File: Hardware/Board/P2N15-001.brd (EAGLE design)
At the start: 72 x 72 mm, 30 parts, among them IC1 TLC5941NT, IC2 LTC485N, IC3 74LS07N, IC4 LTC485N

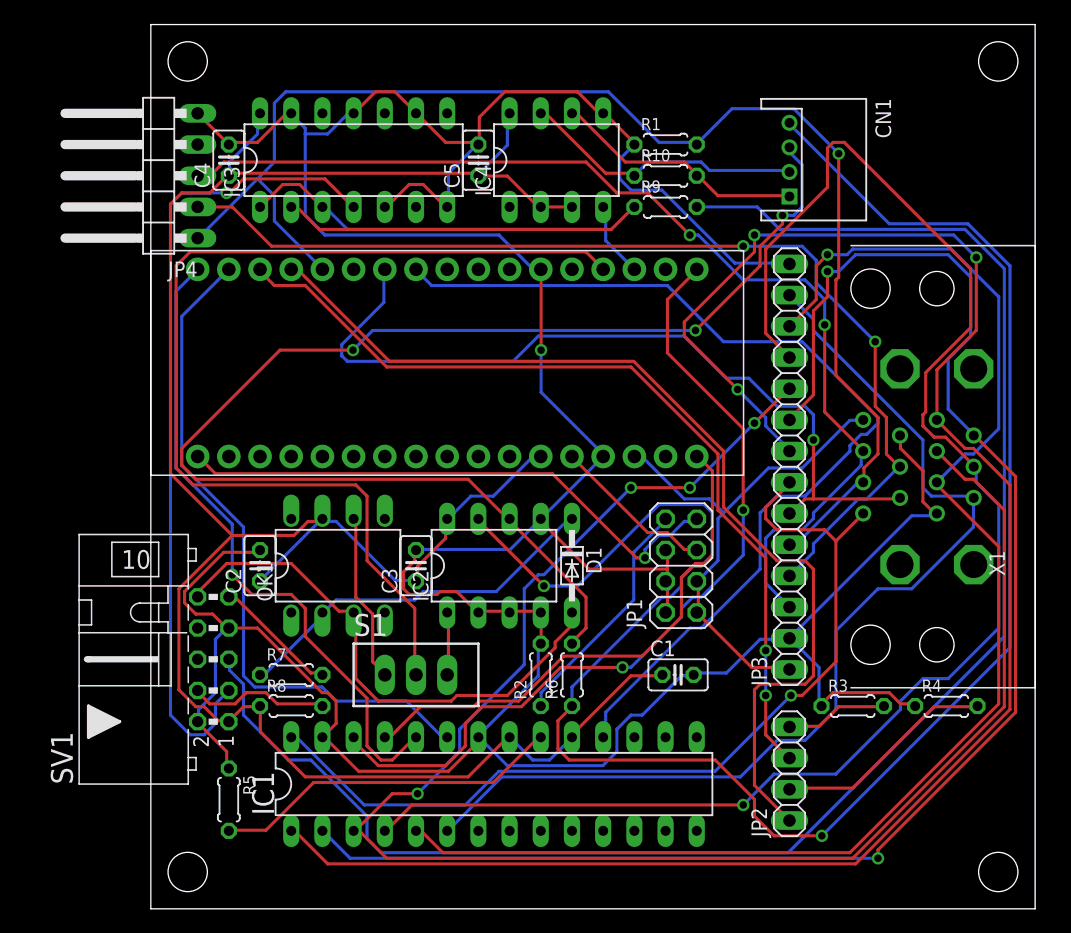
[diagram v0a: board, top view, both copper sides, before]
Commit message: Attached LED pattern to GPIO pins.
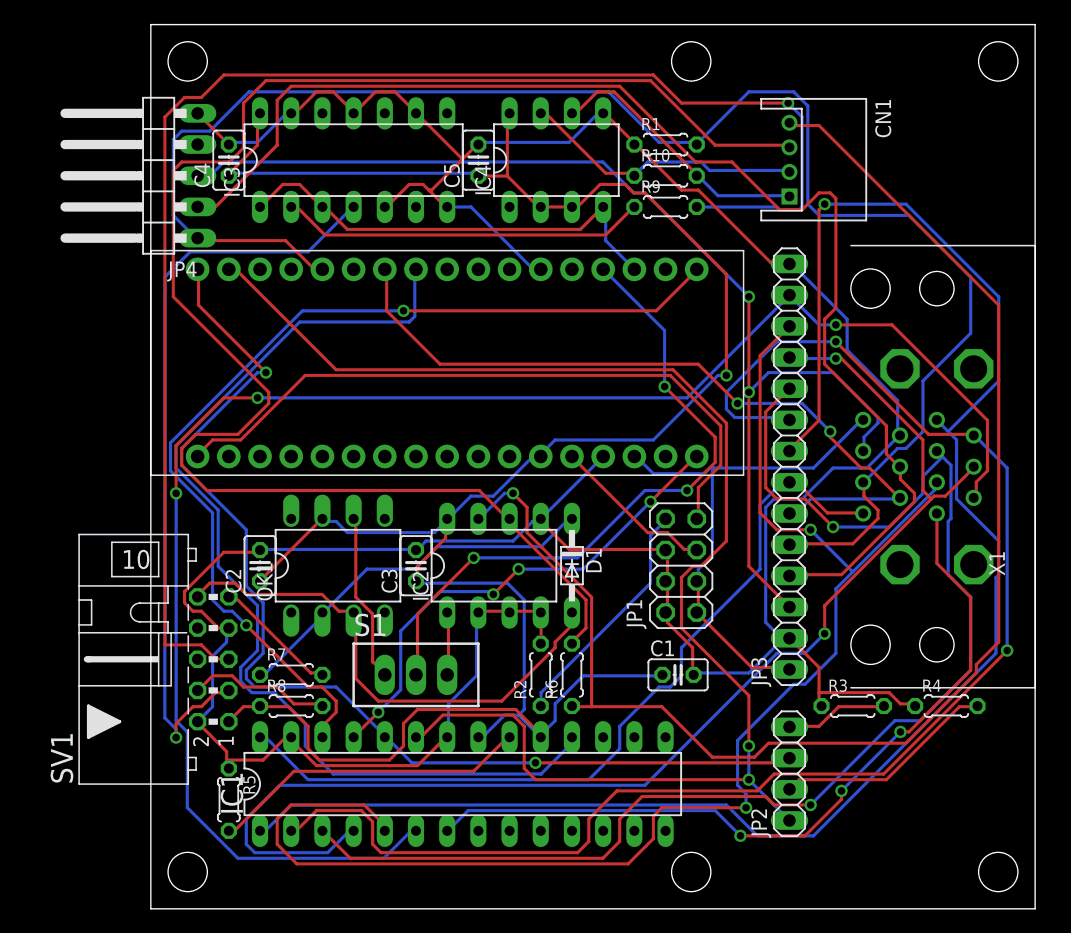
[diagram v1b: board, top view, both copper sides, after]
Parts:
- moved IC1 2.54 mm to (25.4, 10.2)
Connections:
- removed net N$5: JP2.3, MC1.P$3
- new net N$8: IC1.7, X1.14
- net GND: no longer X1.14
- net GPIO1: now also JP2.1
- net GPIO2: now also JP2.3
- net N$3: no longer JP2.1
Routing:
- net N$3: track 81.2 -> 0.00 mm
- net N$5: track 70.8 -> 0.00 mm, vias 2 -> 0
- net N$8: track 0.00 -> 64.0 mm, vias 0 -> 3
- net GPIO1: track 55.5 -> 115.7 mm, vias 0 -> 2
- net N$29: track 83.9 -> 133.3 mm, vias 0 -> 3
- net GND: track 316.0 -> 269.4 mm, vias 1 -> 0
- net GPIO2: track 53.1 -> 89.5 mm, vias 1 -> 2
- net RX-: track 150.4 -> 115.1 mm, vias 2 -> 1
- net RX: track 85.0 -> 53.9 mm, vias 0 -> 3
- net ANLG2: track 137.6 -> 109.3 mm, vias 4 -> 2
- net ANLG3: track 127.3 -> 103.1 mm, vias 1 -> 2
- net RX+: track 108.4 -> 131.6 mm, vias 3 -> 0
- net PD: track 110.9 -> 133.5 mm, vias 1 -> 0
- net USBD-: track 84.9 -> 103.9 mm, vias 2 -> 0
- net RETURN: track 137.1 -> 119.5 mm, vias 0 -> 1
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
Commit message: Added LED monitors to P2N15.
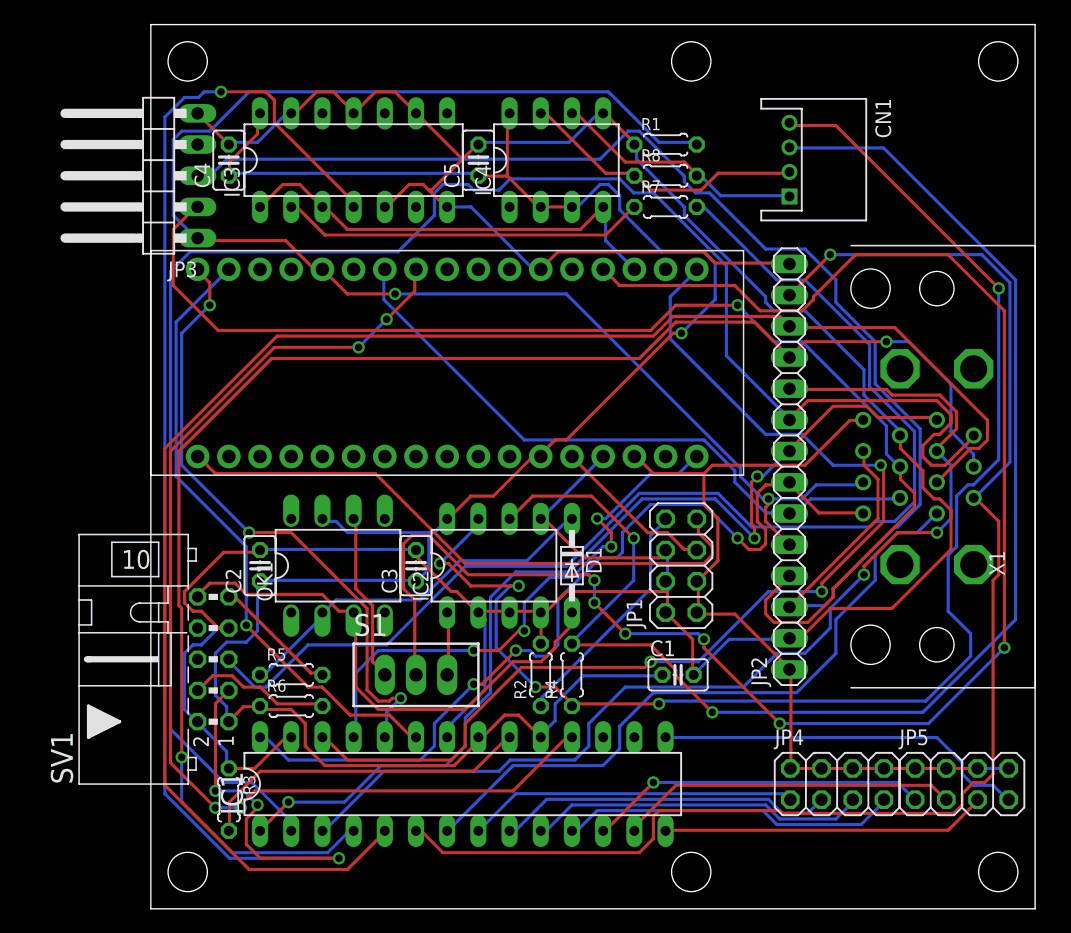
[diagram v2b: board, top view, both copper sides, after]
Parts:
- removed R10: 120, resistor:0204/5
- removed R9: 220, resistor:0204/5
- added JP5: (no value), pinhead:2X04
- JP2: device pinhead:1X04 -> pinhead:1X14
- JP3: device pinhead:1X14 -> pinhead:1X05/90
- JP4: device pinhead:1X05/90 -> pinhead:2X04
- R3: value 330 -> 4.7k
- R4: value 330 -> 120
- R5: value 4.7k -> 220
- R6: value 120 -> 220
- R8: value 220 -> 120
- moved JP4 74.7 mm to (55.9, 10.2), turned to 0 degrees
- moved JP3 57.1 mm to (0.00, 59.7)
- moved R8 52.9 mm to (41.9, 59.7)
- moved R3 51.4 mm to (6.35, 8.89), turned to 270 degrees
- moved R7 48.8 mm to (41.9, 57.1)
- moved R4 30.6 mm to (34.3, 19.1), turned to 90 degrees
- moved JP2 25.0 mm to (52.0, 36.0)
- moved R6 23.0 mm to (11.4, 16.5), turned to 0 degrees
- moved R5 11.4 mm to (11.4, 19.1), turned to 0 degrees
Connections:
- removed net N$6: JP2.2, R4.2
- removed net N$7: JP2.4, R3.2
- new net LED0: IC1.8, JP4.1
- new net LED1: IC1.9, JP4.3
- new net LED2: IC1.10, JP4.5
- new net LED3: IC1.11, JP4.7
- new net LED4: IC1.12, JP5.1
- new net LED5: IC1.13, JP5.3
- new net LED6: IC1.14, JP5.5
- new net LED7: IC1.15, JP5.7
- net ANLG0: now also JP2.8; no longer JP3.8
- net ANLG1: now also JP2.9; no longer JP3.9
- net ANLG2: now also JP2.10; no longer JP3.10
- net ANLG3: now also JP2.11; no longer JP3.11
- net CD: now also JP2.6; no longer JP3.6
- net GND: now also JP2.14, JP2.2, JP3.5; no longer JP3.14, JP3.2, JP4.5, R4.1, R5.1
- net GPIO1: no longer JP2.1
- net GPIO2: no longer JP2.3
- net N$1: now also JP2.7; no longer JP3.7
- net N$15: now also R5.1; no longer R7.1
- net N$2: now also R7.1; no longer R9.1
- net N$28: now also JP2.12; no longer JP3.12
- net N$29: now also JP2.13; no longer JP3.13
- net N$4: now also R3.2; no longer R5.2
- net PD: now also JP2.5, JP3.1; no longer JP3.5, JP4.1
- net RETURN: now also R7.2; no longer R9.2
- net RX+: now also R4.2; no longer R6.2
- net RX-: now also R4.1; no longer R6.1
- net RXA: now also R5.2; no longer R7.2
- net SEND: now also R6.2; no longer R8.2
- net TX+: now also R8.2; no longer R10.2
- net TX-: now also R8.1; no longer R10.1
- net USBD+: now also JP2.3; no longer JP4.3
- net USBD-: now also JP2.4, JP3.2; no longer JP3.4, JP4.2
- net VCC: now also R6.1; no longer R8.1
- net VDD: now also JP2.1, JP4.2, JP4.4, JP4.6, JP4.8, JP5.2, JP5.4, JP5.6, JP5.8; no longer JP3.1
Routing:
- net RX: track 53.9 -> 136.1 mm, vias 3 -> 6
- net GPIO1: track 115.7 -> 50.8 mm, vias 2 -> 1
- net ANLG0: track 140.4 -> 81.5 mm, vias 1 -> 3
- net RAWTX: track 62.2 -> 117.0 mm, vias 1 -> 4
- net GPIO2: track 89.5 -> 50.8 mm, vias 2 -> 3
- net LED7: track 0.00 -> 30.6 mm
- net LED5: track 0.00 -> 27.7 mm
- net LED4: track 0.00 -> 27.6 mm, vias 0 -> 1
- net LED2: track 0.00 -> 27.5 mm
- net LED3: track 0.00 -> 27.5 mm
- net LED1: track 0.00 -> 27.4 mm
- net LED0: track 0.00 -> 26.8 mm
- net LED6: track 0.00 -> 26.5 mm
- net VDD: track 42.9 -> 69.0 mm
- net ANLG1: track 120.0 -> 142.8 mm, vias 2 -> 0
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
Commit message: Added Reset SW.
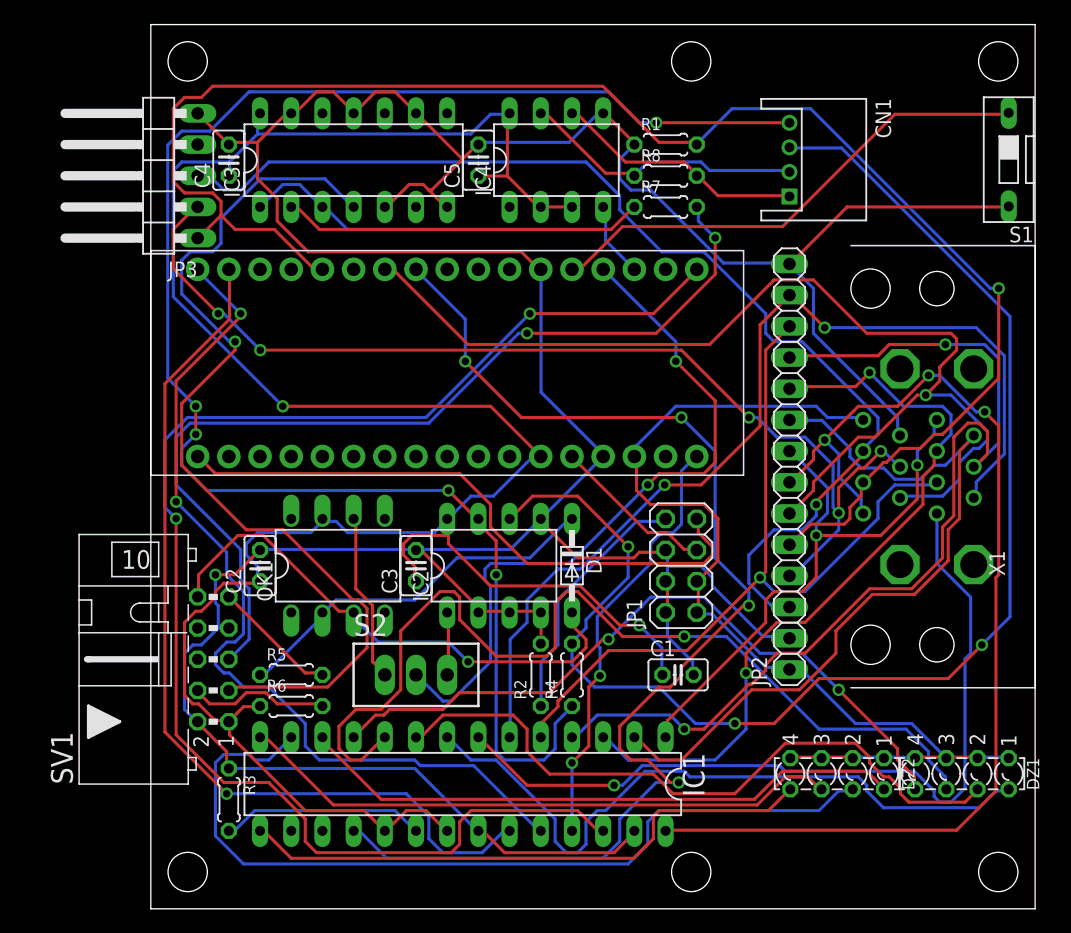
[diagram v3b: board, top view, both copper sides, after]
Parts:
- removed JP4, JP5: (no value), pinhead:2X04
- added DZ1, DZ2: LZR184, led:LZR184
- added S2: TL36PO, switch:TL3XPO
- S1: value TL36PO -> (none); device switch:TL3XPO -> switch-dil:DS-01
- moved S1 63.9 mm to (69.8, 61.0), turned to 180 degrees
- turned IC1 to 180 degrees
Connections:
- new net N$5: MC1.P$22, S1.1
- net GND: now also S1.2
- net LED0: now also DZ1.K1; no longer JP4.1
- net LED1: now also DZ1.K2; no longer JP4.3
- net LED2: now also DZ1.K3; no longer JP4.5
- net LED3: now also DZ1.K4; no longer JP4.7
- net LED4: now also DZ2.K1; no longer JP5.1
- net LED5: now also DZ2.K2; no longer JP5.3
- net LED6: now also DZ2.K3; no longer JP5.5
- net LED7: now also DZ2.K4; no longer JP5.7
- net MIDIRX: now also S2.1; no longer S1.1
- net RX: now also S2.2; no longer S1.2
- net VDD: now also DZ1.A1, DZ1.A2, DZ1.A3, DZ1.A4, DZ2.A1, DZ2.A2, DZ2.A3, DZ2.A4; no longer JP4.2, JP4.4, JP4.6, JP4.8, JP5.2, JP5.4, JP5.6, JP5.8
- net XMIDIRX: now also S2.3; no longer S1.3
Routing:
- net ANLG1: track 142.8 -> 64.1 mm
- net RX: track 136.1 -> 57.9 mm, vias 6 -> 2
- net N$28: track 131.6 -> 64.9 mm, vias 0 -> 1
- net LED2: track 27.5 -> 78.7 mm, vias 0 -> 1
- net LED5: track 27.7 -> 69.9 mm
- net RAWTX: track 117.0 -> 75.3 mm, vias 4 -> 1
- net N$5: track 0.00 -> 40.9 mm
- net ANLG3: track 123.1 -> 82.3 mm
- net CD: track 52.7 -> 91.2 mm, vias 0 -> 1
- net N$29: track 114.8 -> 80.5 mm, vias 1 -> 2
- net ANLG0: track 81.5 -> 48.1 mm, vias 3 -> 2
- net GND: track 272.7 -> 303.8 mm, vias 0 -> 1
- net LED3: track 27.5 -> 58.0 mm, vias 0 -> 2
- net LED0: track 26.8 -> 56.6 mm
- net MOSI: track 88.6 -> 116.5 mm, vias 3 -> 2
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
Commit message: Added MIDI THRU function.
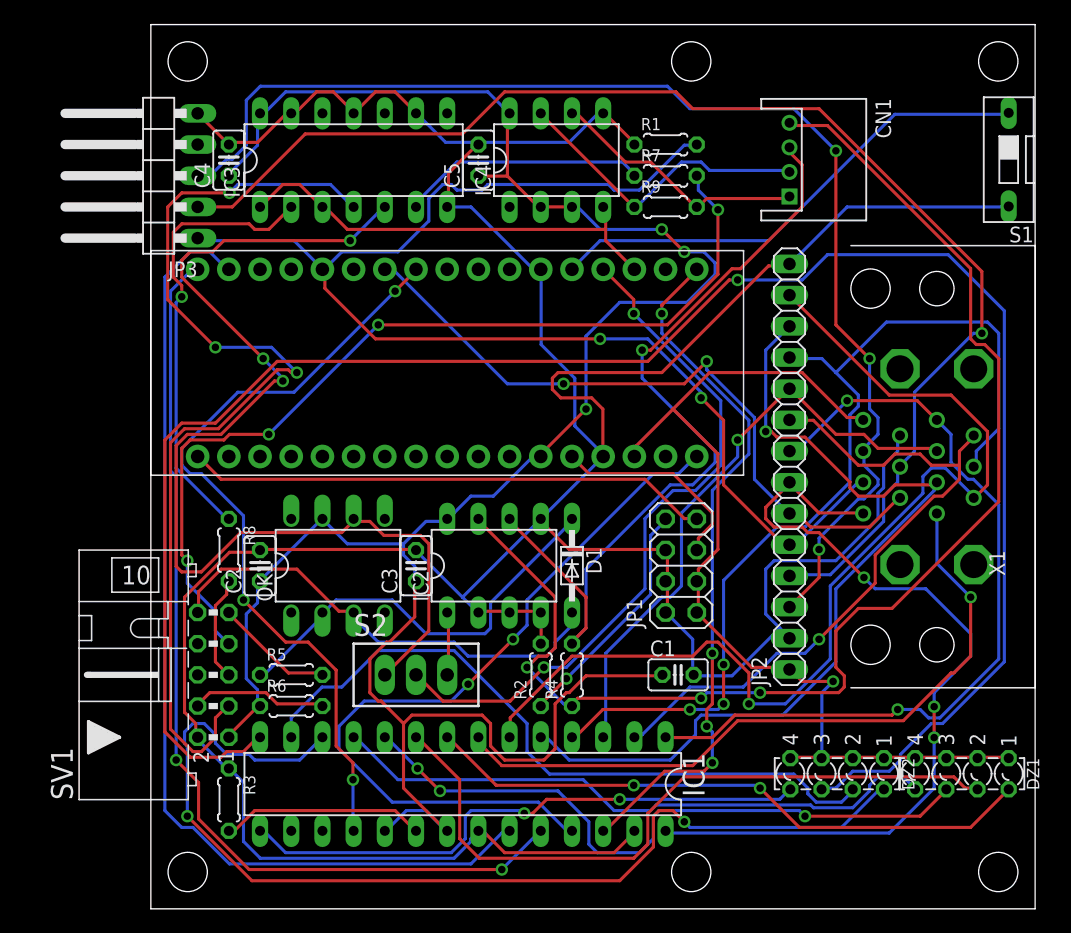
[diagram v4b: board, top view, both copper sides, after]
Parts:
- added R9: 120, resistor:0204/5
- R8: value 120 -> 220
- moved R8 46.8 mm to (6.35, 29.2), turned to 270 degrees
- moved R7 2.54 mm to (41.9, 59.7)
- moved SV1 1.27 mm to (5.08, 19.1)
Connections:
- new net N$6: IC3.6, R7.1
- new net N$7: R7.2, SV1.7
- net GND: no longer IC3.5, SV1.7
- net MIDIRX: now also IC3.5
- net N$2: now also R8.1; no longer R7.1
- net RETURN: now also R8.2; no longer R7.2
- net TX+: now also R9.2; no longer R8.2
- net TX-: now also R9.1; no longer R8.1
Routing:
- net LED6: track 49.4 -> 157.6 mm, vias 0 -> 1
- net N$7: track 0.00 -> 75.8 mm, vias 0 -> 4
- net MIDIRX: track 13.7 -> 87.9 mm, vias 0 -> 3
- net RETURN: track 76.8 -> 8.54 mm, vias 2 -> 0
- net MOSI: track 116.5 -> 57.1 mm, vias 2 -> 4
- net RX+: track 113.0 -> 68.6 mm, vias 3 -> 1
- net GPIO0: track 100.0 -> 63.7 mm, vias 4 -> 3
- net LED4: track 49.7 -> 85.5 mm, vias 0 -> 2
- net CD: track 91.2 -> 56.5 mm, vias 1 -> 2
- net RX-: track 136.1 -> 106.5 mm, vias 5 -> 3
- net SCLK: track 35.5 -> 63.0 mm
- net PD: track 132.7 -> 107.3 mm, vias 1 -> 2
- net LED2: track 78.7 -> 54.3 mm, vias 1 -> 3
- net USBD-: track 86.2 -> 107.4 mm, vias 5 -> 1
- net N$6: track 0.00 -> 20.1 mm
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
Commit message: Updated Hirose DX10LM1-14SE connector pattern.
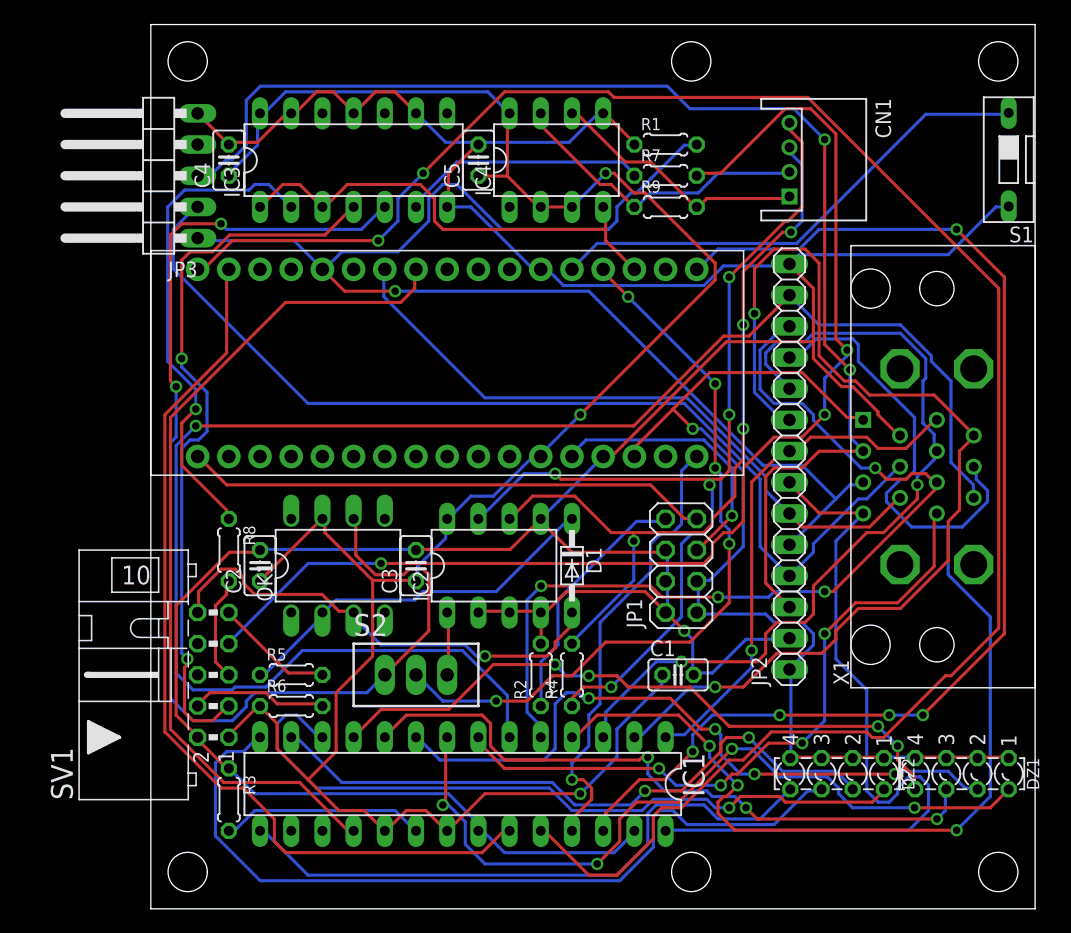
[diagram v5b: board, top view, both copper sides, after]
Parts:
- X1: value (none) -> HIROSE-DX10LM1-14SE; device con-hirose-dxlm:HIROSE-DXLM -> con-hirose-dx10lm1-14se:HIROSE-DX10LM1-14SE
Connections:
- net ANLG0: now also X1.P$8; no longer X1.8
- net ANLG1: now also X1.P$9; no longer X1.9
- net ANLG2: now also X1.P$10; no longer X1.10
- net ANLG3: now also X1.P$11; no longer X1.11
- net CD: now also X1.P$6; no longer X1.6
- net GND: now also X1.P$2; no longer X1.2
- net N$1: now also X1.P$7; no longer X1.7
- net N$28: now also X1.P$12; no longer X1.12
- net N$29: now also X1.P$13; no longer X1.13
- net N$8: now also X1.P$14; no longer X1.14
- net PD: now also X1.P$5; no longer X1.5
- net USBD+: now also X1.P$3; no longer X1.3
- net USBD-: now also X1.P$4; no longer X1.4
- net VDD: now also X1.P$1; no longer X1.1
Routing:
- net LED6: track 157.6 -> 66.8 mm, vias 1 -> 0
- net GPIO2: track 77.7 -> 155.2 mm
- net N$29: track 85.4 -> 134.0 mm
- net MOSI: track 57.1 -> 97.9 mm, vias 4 -> 5
- net ANLG1: track 56.7 -> 86.1 mm, vias 1 -> 2
- net RX-: track 106.5 -> 78.9 mm, vias 3 -> 5
- net SCLK: track 63.0 -> 37.1 mm, vias 2 -> 1
- net LED4: track 85.5 -> 60.1 mm, vias 2 -> 1
- net ANLG3: track 78.6 -> 103.2 mm
- net USBD-: track 107.4 -> 82.7 mm, vias 1 -> 0
- net ANLG0: track 66.5 -> 42.4 mm, vias 2 -> 1
- net N$7: track 75.8 -> 97.8 mm, vias 4 -> 3
- net RAWTX: track 81.3 -> 59.4 mm, vias 3 -> 2
- net ANLG2: track 49.2 -> 68.0 mm, vias 1 -> 2
- net LED0: track 50.0 -> 62.7 mm, vias 2 -> 4
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
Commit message: Changed R value of main LED (from 220 to 150 ohm).
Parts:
- R2: value 220 -> 150
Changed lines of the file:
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@@
 <element name="R5" library="resistor" package="0204/5" value="220" x="11.43" y="19.05"/>
 <element name="MC1" library="adafruit" package="ARDUINOMICRO" value="ARDUINOMICRO" x="24.13" y="44.45"/>
-<element name="R2" library="resistor" package="0204/5" value="220" x="31.75" y="19.05" rot="R90"/>
+<element name="R2" library="resistor" package="0204/5" value="150" x="31.75" y="19.05" rot="R90"/>
 <element name="SV1" library="con-ml" package="ML10L" value="" x="5.08" y="19.05" rot="R90">
 <attribute name="OC_NEWARK" value="unknown" x="5.08" y="19.05" size="1.778" layer="27" rot="R90" display="off"/>
